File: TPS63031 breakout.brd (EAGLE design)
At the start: 17.8 x 15.9 mm, 10 parts, among them IC1 PESD5V2S2UT, IC2 TPS63001DRCR

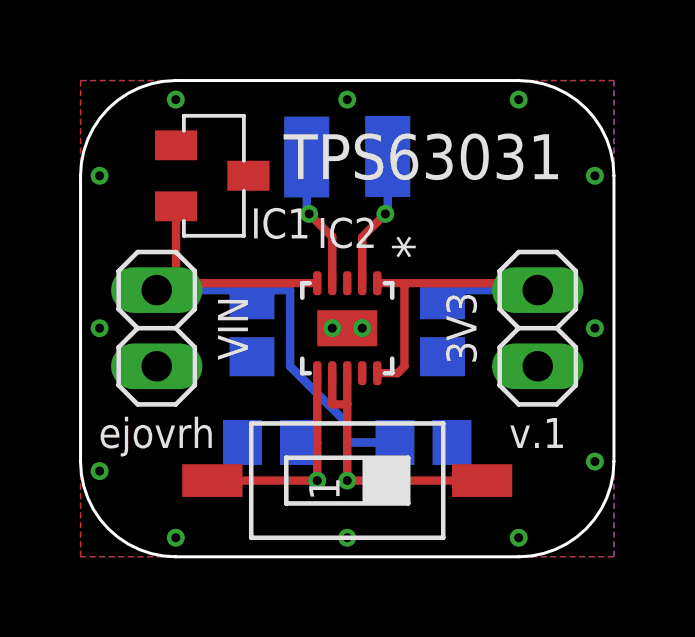
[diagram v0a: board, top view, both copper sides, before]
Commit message: - updated TPS63031 device name & redo of gerbers - added BOM
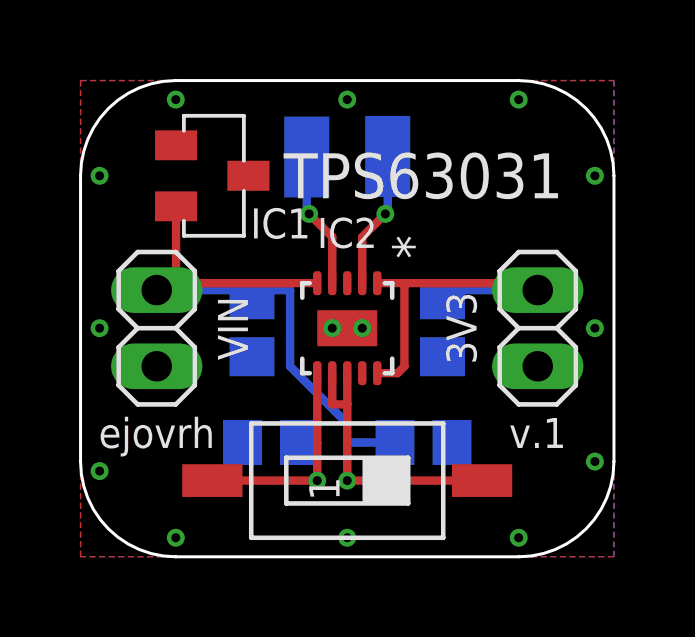
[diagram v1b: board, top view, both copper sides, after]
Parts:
- IC2: value TPS63001DRCR -> TPS63031DSKT
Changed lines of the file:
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@@
 <?xml version="1.0" encoding="utf-8"?>
 <!DOCTYPE eagle SYSTEM "eagle.dtd">
-<eagle version="8.3.2">
+<eagle version="8.5.0">
 <drawing>
 <settings>
@@
 <board>
 <plain>
-<text x="17.78" y="19.685" size="1.5" layer="21" font="vector" align="center">TPS63031</text>
+<text x="17.78" y="19.05" size="1.5" layer="21" font="vector" align="center">TPS63031</text>
 <wire x1="9.525" y1="22.225" x2="20.955" y2="22.225" width="0.1" layer="20"/>
 <wire x1="24.13" y1="19.05" x2="24.13" y2="9.525" width="0.1" layer="20"/>
@@
 <param name="dpMaxLengthDifference" value="10mm"/>
 <param name="dpGapFactor" value="2.5"/>
-<param name="checkGrid" value="0"/>
 <param name="checkAngle" value="1"/>
 <param name="checkFont" value="0"/>
 <param name="checkRestrict" value="1"/>
+<param name="checkStop" value="0"/>
+<param name="checkValues" value="0"/>
 <param name="useDiameter" value="13"/>
 <param name="maxErrors" value="50"/>
@@
 <attribute name="VALUE" x="15.875" y="12.7" size="1.27" layer="28" rot="MR90"/>
 </element>
-<element name="IC2" library="TPS63031 - Buck Boost Voltage Regulator" package="SMT" value="TPS63001DRCR" x="15.24" y="13.97" smashed="yes" rot="R270">
+<element name="IC2" library="TPS63031 - Buck Boost Voltage Regulator" package="SMT" value="TPS63031DSKT" x="15.24" y="13.97" smashed="yes" rot="R270">
 <attribute name="NAME" x="15.24" y="17.145" size="1" layer="25" font="vector" ratio="6" rot="SR0" align="center"/>
 <attribute name="VALUE" x="11.772" y="15.5194" size="1.27" layer="27" ratio="6" rot="SR270"/>

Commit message: - added + and - markings on in and out - improved ground traces
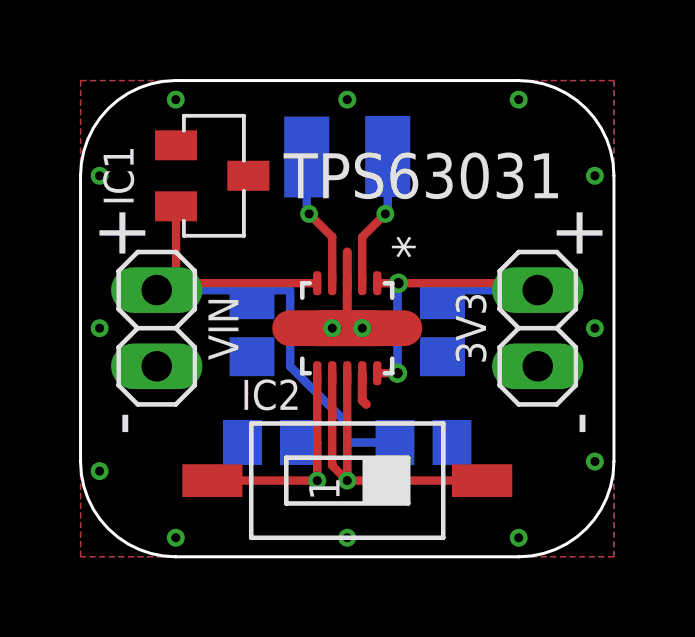
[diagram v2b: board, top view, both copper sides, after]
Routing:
- net GND: track 0.00 -> 6.81 mm
- net VIN: track 31.7 -> 33.9 mm
- net 3V3: track 12.5 -> 12.4 mm, vias 0 -> 2
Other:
- board text added: "+"
- board text added: "-"
- board text added: "v.2"
- board text removed: "v.1"
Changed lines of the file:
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@@
 <setting verticaltext="up"/>
 </settings>
-<grid distance="12.5" unitdist="mil" unit="mm" style="dots" multiple="1" display="yes" altdistance="5" altunitdist="mil" altunit="mm"/>
+<grid distance="25" unitdist="mil" unit="mil" style="dots" multiple="1" display="yes" altdistance="0.1" altunitdist="mm" altunit="mm"/>
 <layers>
 <layer number="1" name="Top" color="4" fill="1" visible="yes" active="yes"/>
@@
 <wire x1="20.955" y1="6.35" x2="24.13" y2="9.525" width="0.1" layer="20" curve="90"/>
 <wire x1="6.35" y1="9.525" x2="9.525" y2="6.35" width="0.1" layer="20" curve="90"/>
-<text x="8.89" y="10.4775" size="1" layer="21" font="vector" align="center">ejovrh</text>
-<text x="21.59" y="10.4775" size="1" layer="21" font="vector" align="center">v.1</text>
+<text x="17.4625" y="16.8275" size="1" layer="22" font="vector" rot="MR0" align="center">ejovrh</text>
+<text x="11.7475" y="16.8275" size="1" layer="22" font="vector" rot="MR0" align="center">v.2</text>
+<text x="7.62" y="17.145" size="1.778" layer="21" font="vector" rot="R90" align="center">+</text>
+<text x="7.62" y="10.795" size="1.778" layer="21" font="vector" rot="R90" align="center">-</text>
+<text x="22.86" y="17.145" size="1.778" layer="21" font="vector" rot="R270" align="center">+</text>
+<text x="22.86" y="10.795" size="1.778" layer="21" font="vector" rot="R270" align="center">-</text>
+<text x="7.62" y="17.145" size="1.778" layer="22" font="vector" rot="MR270" align="center">+</text>
+<text x="22.86" y="17.145" size="1.778" layer="22" font="vector" rot="MR90" align="center">+</text>
+<text x="22.86" y="10.795" size="1.778" layer="22" font="vector" rot="MR270" align="center">-</text>
+<text x="7.62" y="10.795" size="1.778" layer="22" font="vector" rot="MR270" align="center">-</text>
 </plain>
 <attributes>
@@
 </element>
 <element name="IC2" library="TPS63031 - Buck Boost Voltage Regulator" package="SMT" value="TPS63031DSKT" x="15.24" y="13.97" smashed="yes" rot="R270">
-<attribute name="NAME" x="15.24" y="17.145" size="1" layer="25" font="vector" ratio="6" rot="SR0" align="center"/>
+<attribute name="NAME" x="12.7" y="11.7475" size="1" layer="25" font="vector" ratio="6" rot="SR0" align="center"/>
 <attribute name="VALUE" x="11.772" y="15.5194" size="1.27" layer="27" ratio="6" rot="SR270"/>
 </element>
 <element name="3V3" library="pinhead" library_urn="urn:adsk.eagle:library:325" package="1X02" package3d_urn="urn:adsk.eagle:package:22435/2" value="" x="21.59" y="13.97" smashed="yes" rot="R90">
-<attribute name="NAME" x="19.05" y="13.97" size="1" layer="25" font="vector" rot="R90" align="center"/>
+<attribute name="NAME" x="19.3675" y="13.97" size="1" layer="25" font="vector" rot="R90" align="center"/>
 <attribute name="VALUE" x="24.765" y="11.43" size="1.27" layer="27" rot="R90"/>
 </element>
 <element name="L1" library="DJNR3015-1R5 Inductor" package="FFF" value="DJNR3015-2R2" x="15.24" y="19.685" smashed="yes" rot="MR0">
-<attribute name="NAME" x="15.065" y="16.335" size="1" layer="22" font="vector" rot="MR0" align="center"/>
+<attribute name="NAME" x="19.05" y="19.685" size="1" layer="22" font="vector" rot="MR270" align="center"/>
 </element>
 <element name="R1" library="resistor" library_urn="urn:adsk.eagle:library:348" package="R0805" value="10k" x="12.7" y="10.16" smashed="yes" rot="MR180">
@@
 </element>
 <element name="VIN" library="pinhead" library_urn="urn:adsk.eagle:library:325" package="1X02" package3d_urn="urn:adsk.eagle:package:22435/2" value="" x="8.89" y="13.97" smashed="yes" rot="R270">
-<attribute name="NAME" x="11.43" y="13.97" size="1" layer="25" font="vector" rot="R270" align="center"/>
+<attribute name="NAME" x="11.1125" y="13.97" size="1" layer="25" font="vector" rot="R270" align="center"/>
 <attribute name="VALUE" x="5.715" y="16.51" size="1.27" layer="27" rot="R270"/>
 </element>
 <element name="IC1" library="PESDxS2UT" package="SOT-23" value="PESD5V2S2UT" x="10.795" y="19.05" smashed="yes" rot="R270">
-<attribute name="NAME" x="13.0175" y="17.4625" size="1" layer="21" font="vector" align="center"/>
+<attribute name="NAME" x="7.62" y="19.05" size="1" layer="21" font="vector" rot="R270" align="center"/>
 </element>
 </elements>
@@
 <contactref element="IC1" pad="CH2"/>
 <wire x1="19.7358" y1="8.89" x2="15.24" y2="8.89" width="0.2794" layer="1"/>
-<wire x1="15.24" y1="8.89" x2="15.24" y2="11.43" width="0.2794" layer="1"/>
-<wire x1="15.24" y1="11.43" x2="15.24" y2="12.470003125" width="0.2794" layer="1"/>
-<wire x1="15.24" y1="11.43" x2="14.74" y2="11.43" width="0.2794" layer="1"/>
-<wire x1="14.74" y1="11.43" x2="14.74" y2="12.470003125" width="0.2794" layer="1"/>
+<wire x1="15.24" y1="8.89" x2="15.24" y2="12.470003125" width="0.2794" layer="1"/>
+<wire x1="15.24" y1="11.43" x2="15.24" y2="12.470003125" width="0" layer="19" extent="1-16"/>
+<wire x1="15.24" y1="11.43" x2="14.74" y2="11.43" width="0" layer="19" extent="1-16"/>
+<wire x1="14.74" y1="11.43" x2="14.74" y2="12.065" width="0" layer="19" extent="1-16"/>
 <via x="15.24" y="8.89" extent="1-16" drill="0.3"/>
+<wire x1="14.74" y1="12.065" x2="14.74" y2="12.470003125" width="0" layer="19" extent="1-16"/>
 <wire x1="9.525" y1="15.469996875" x2="14.240003125" y2="15.469996875" width="0.2794" layer="1"/>
 <wire x1="9.525" y1="15.469996875" x2="9.119996875" y2="15.469996875" width="0.2794" layer="1"/>
@@
 <wire x1="13.335" y1="15.24" x2="11.905" y2="15.24" width="0.2794" layer="16"/>
 <wire x1="11.905" y1="15.24" x2="11.905" y2="15.08" width="0.2794" layer="16"/>
+<wire x1="15.24" y1="8.89" x2="14.74" y2="9.39" width="0.2794" layer="1"/>
+<wire x1="14.74" y1="9.39" x2="14.74" y2="12.470003125" width="0.2794" layer="1"/>
 </signal>
 <signal name="3V3">
@@
 <contactref element="C3" pad="2"/>
 <contactref element="3V3" pad="2"/>
-<wire x1="21.360003125" y1="15.469996875" x2="17.145" y2="15.469996875" width="0.2794" layer="1"/>
+<wire x1="21.360003125" y1="15.469996875" x2="16.945" y2="15.469996875" width="0.2794" layer="1"/>
 <wire x1="21.360003125" y1="15.469996875" x2="21.59" y2="15.24" width="0.2794" layer="1"/>
 <wire x1="21.59" y1="15.24" x2="18.735" y2="15.24" width="0.2794" layer="16"/>
 <wire x1="18.735" y1="15.24" x2="18.415" y2="14.92" width="0.2794" layer="16"/>
-<wire x1="17.145" y1="12.7" x2="17.145" y2="15.469996875" width="0.2794" layer="1"/>
+<wire x1="16.945" y1="15.469996875" x2="16.239996875" y2="15.469996875" width="0.2794" layer="1"/>
 <wire x1="16.239996875" y1="12.470003125" x2="16.915003125" y2="12.470003125" width="0.2794" layer="1"/>
-<wire x1="16.915003125" y1="12.470003125" x2="17.145" y2="12.7" width="0.2794" layer="1"/>
-<wire x1="17.145" y1="15.469996875" x2="16.239996875" y2="15.469996875" width="0.2794" layer="1"/>
+<via x="16.915003125" y="12.470003125" extent="1-16" drill="0.35"/>
+<via x="16.945" y="15.469996875" extent="1-16" drill="0.35"/>
+<wire x1="16.915003125" y1="12.470003125" x2="16.915003125" y2="15.44" width="0.2794" layer="16"/>
+<wire x1="16.915003125" y1="15.44" x2="16.945" y2="15.469996875" width="0.2794" layer="16"/>
 </signal>
 <signal name="GND">
@@
 <via x="6.985" y="13.97" extent="1-16" drill="0.3"/>
 <via x="23.495" y="13.97" extent="1-16" drill="0.3"/>
+<wire x1="15.24" y1="13.97" x2="13.335" y2="13.97" width="1.1938" layer="1"/>
+<wire x1="15.24" y1="13.97" x2="17.145" y2="13.97" width="1.1938" layer="1"/>
+<wire x1="15.24" y1="15.469996875" x2="15.24" y2="16.51" width="0.3048" layer="1"/>
+<wire x1="15.24" y1="15.469996875" x2="15.24" y2="14.605" width="0.3048" layer="1"/>
+<wire x1="15.74" y1="12.470003125" x2="15.74" y2="11.565" width="0.3048" layer="1"/>
+<wire x1="15.74" y1="11.565" x2="15.875" y2="11.43" width="0.3048" layer="1"/>
 </signal>
 <signal name="N$3">

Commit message: - adjusted board dimensions & updated gerbers
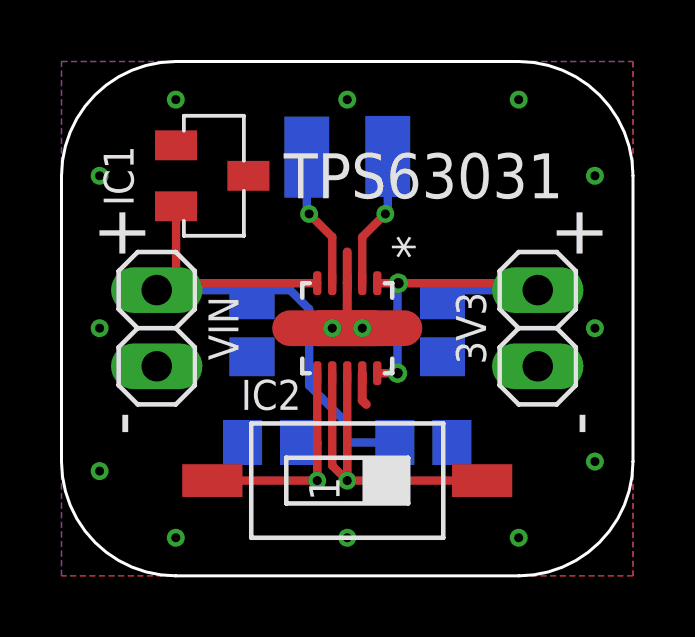
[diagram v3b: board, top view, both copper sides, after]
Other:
- board size 17.8 x 15.9 mm -> 19.1 x 17.1 mm
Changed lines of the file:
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@@
 <setting verticaltext="up"/>
 </settings>
-<grid distance="25" unitdist="mil" unit="mil" style="dots" multiple="1" display="yes" altdistance="0.1" altunitdist="mm" altunit="mm"/>
+<grid distance="25" unitdist="mil" unit="mm" style="dots" multiple="1" display="yes" altdistance="0.1" altunitdist="mm" altunit="mm"/>
 <layers>
 <layer number="1" name="Top" color="4" fill="1" visible="yes" active="yes"/>
@@
 <plain>
 <text x="17.78" y="19.05" size="1.5" layer="21" font="vector" align="center">TPS63031</text>
-<wire x1="9.525" y1="22.225" x2="20.955" y2="22.225" width="0.1" layer="20"/>
-<wire x1="24.13" y1="19.05" x2="24.13" y2="9.525" width="0.1" layer="20"/>
-<wire x1="20.955" y1="6.35" x2="9.525" y2="6.35" width="0.1" layer="20"/>
-<wire x1="6.35" y1="9.525" x2="6.35" y2="19.05" width="0.1" layer="20"/>
-<wire x1="9.525" y1="22.225" x2="6.35" y2="19.05" width="0.1" layer="20" curve="90"/>
-<wire x1="24.13" y1="19.05" x2="20.955" y2="22.225" width="0.1" layer="20" curve="90"/>
-<wire x1="20.955" y1="6.35" x2="24.13" y2="9.525" width="0.1" layer="20" curve="90"/>
-<wire x1="6.35" y1="9.525" x2="9.525" y2="6.35" width="0.1" layer="20" curve="90"/>
+<wire x1="9.525" y1="22.86" x2="20.955" y2="22.86" width="0.1" layer="20"/>
+<wire x1="24.765" y1="19.05" x2="24.765" y2="9.525" width="0.1" layer="20"/>
+<wire x1="20.955" y1="5.715" x2="9.525" y2="5.715" width="0.1" layer="20"/>
+<wire x1="5.715" y1="9.525" x2="5.715" y2="19.05" width="0.1" layer="20"/>
+<wire x1="9.525" y1="22.86" x2="5.715" y2="19.05" width="0.1" layer="20" curve="90"/>
+<wire x1="24.765" y1="19.05" x2="20.955" y2="22.86" width="0.1" layer="20" curve="90"/>
+<wire x1="20.955" y1="5.715" x2="24.765" y2="9.525" width="0.1" layer="20" curve="90"/>
+<wire x1="5.715" y1="9.525" x2="9.525" y2="5.715" width="0.1" layer="20" curve="90"/>
 <text x="17.4625" y="16.8275" size="1" layer="22" font="vector" rot="MR0" align="center">ejovrh</text>
 <text x="11.7475" y="16.8275" size="1" layer="22" font="vector" rot="MR0" align="center">v.2</text>
@@
 <text x="22.86" y="10.795" size="1.778" layer="22" font="vector" rot="MR270" align="center">-</text>
 <text x="7.62" y="10.795" size="1.778" layer="22" font="vector" rot="MR270" align="center">-</text>
+<dimension x1="5.715" y1="9.525" x2="24.765" y2="9.525" x3="15.24" y3="0.635" textsize="1.778" layer="48"/>
+<dimension x1="20.955" y1="22.86" x2="20.955" y2="5.715" x3="28.574996875" y3="14.2875" textsize="1.778" layer="48"/>
 </plain>
 <attributes>
@@
 <param name="mdViaViaSameLayer" value="8mil"/>
 <param name="mnLayersViaInSmd" value="2"/>
-<param name="mdCopperDimension" value="0mil"/>
+<param name="mdCopperDimension" value="16mil"/>
 <param name="mdDrill" value="8mil"/>
 <param name="mdSmdStop" value="0mil"/>
@@
 <wire x1="19.7358" y1="8.89" x2="15.24" y2="8.89" width="0.2794" layer="1"/>
 <wire x1="15.24" y1="8.89" x2="15.24" y2="12.470003125" width="0.2794" layer="1"/>
-<wire x1="15.24" y1="11.43" x2="15.24" y2="12.470003125" width="0" layer="19" extent="1-16"/>
-<wire x1="15.24" y1="11.43" x2="14.74" y2="11.43" width="0" layer="19" extent="1-16"/>
-<wire x1="14.74" y1="11.43" x2="14.74" y2="12.065" width="0" layer="19" extent="1-16"/>
 <via x="15.24" y="8.89" extent="1-16" drill="0.3"/>
-<wire x1="14.74" y1="12.065" x2="14.74" y2="12.470003125" width="0" layer="19" extent="1-16"/>
 <wire x1="9.525" y1="15.469996875" x2="14.240003125" y2="15.469996875" width="0.2794" layer="1"/>
 <wire x1="9.525" y1="15.469996875" x2="9.119996875" y2="15.469996875" width="0.2794" layer="1"/>
@@
 <wire x1="16.83" y1="10.16" x2="15.24" y2="10.16" width="0.2794" layer="16"/>
 <wire x1="15.24" y1="10.16" x2="15.24" y2="10.795" width="0.2794" layer="16"/>
-<wire x1="15.24" y1="10.795" x2="13.335" y2="12.7" width="0.2794" layer="16"/>
-<wire x1="13.335" y1="12.7" x2="13.335" y2="15.24" width="0.2794" layer="16"/>
+<wire x1="15.24" y1="10.795" x2="13.97" y2="12.065" width="0.2794" layer="16"/>
 <wire x1="12.38" y1="14.605" x2="12.065" y2="14.92" width="0.2794" layer="16"/>
 <wire x1="13.335" y1="15.24" x2="11.905" y2="15.24" width="0.2794" layer="16"/>
@@
 <wire x1="15.24" y1="8.89" x2="14.74" y2="9.39" width="0.2794" layer="1"/>
 <wire x1="14.74" y1="9.39" x2="14.74" y2="12.470003125" width="0.2794" layer="1"/>
+<wire x1="13.97" y1="12.065" x2="13.97" y2="14.605" width="0.2794" layer="16"/>
+<wire x1="13.97" y1="14.605" x2="13.335" y2="15.24" width="0.2794" layer="16"/>
 </signal>
 <signal name="3V3">
@@
 <contactref element="IC1" pad="GND"/>
 <polygon width="0.1" layer="16">
-<vertex x="6.35" y="22.225"/>
-<vertex x="24.13" y="22.225"/>
-<vertex x="24.13" y="6.35"/>
-<vertex x="6.35" y="6.35"/>
+<vertex x="5.715" y="22.86"/>
+<vertex x="24.765" y="22.86"/>
+<vertex x="24.765" y="5.715"/>
+<vertex x="5.715" y="5.715"/>
 </polygon>
 <polygon width="0.1" layer="1">
-<vertex x="6.35" y="22.225"/>
-<vertex x="24.13" y="22.225"/>
-<vertex x="24.13" y="6.35"/>
-<vertex x="6.35" y="6.35"/>
+<vertex x="5.715" y="22.86"/>
+<vertex x="24.765" y="22.86"/>
+<vertex x="24.765" y="5.715"/>
+<vertex x="5.715" y="5.715"/>
 </polygon>
 <via x="9.525" y="21.59" extent="1-16" drill="0.3"/>
